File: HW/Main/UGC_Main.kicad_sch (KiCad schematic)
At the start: 147 parts, among them J1 Rumble, J1 USB4105-GF-A-060, J10 Conn_01x01_Pin, J11 Conn_01x01_Pin, J12 Conn_01x01_Pin, J2 LT, J3 RT, J5 Conn_01x01_Pin, J6 Conn_01x01_Pin, J7 Conn_01x01_Pin, J7 Conn_01x05_Pin, J8 Conn_01x01_Pin, J9 Conn_01x01_Pin, J9 Conn_01x05_Pin, Q1 MMBT3904, Q2 MMBT3904, Q3 BSS138DW, Q4 BSS138DW, Q5 Q_NMOS_GSD, Q6 Q_PMOS_GDS, Q7 Q_NMOS_GSD, SW1 SW_Push, SW10 SW_Push, SW11 SW_Push, SW12 SW_Push, SW13 SW_Push, SW14 TS09-63-25-R-260-SMT, SW2 SW_Push, SW3 SW_Push, SW4 SW_Push, SW5 SW_Push, SW6 GL18_SW, SW7 SW_Push, SW8 SW_Push, SW9 TS09-63-25-R-260-SMT, T1 36-8730, T2 36-8730, T3 36-8730, T4 36-8730, U1 ESP32-PICO-MINI-02, U10 ST_LSM6, U11 BQ25180, U12 CH340K, U13 PI3USB4000A, U14 GH39F (Hall SOT23), U15 GH39F (Hall SOT23), U16 GH39F (Hall SOT23), U17 GH39F (Hall SOT23), U2 GD25Q80EEIGR, U2 GH39F (Hall SOT23), U3 GH39F (Hall SOT23), U4 GH39F (Hall SOT23), U5 GH39F (Hall SOT23), U6 MCP3002, U7 MCP3002, U8 RP2040, Y1 Crystal_GND3

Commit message: Checkpoint 2
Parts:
- removed C23, C24, C25, C26, C4: .047u, Capacitor_SMD:C_0603_1608Metric_Pad1.08x0.95mm_HandSolder, symbol Device:C
- removed J7: Conn_01x05_Pin, hhl:molex_5034800540, symbol Connector:Conn_01x05_Pin
- removed J9: Conn_01x05_Pin, Connector_PinHeader_2.00mm:PinHeader_1x05_P2.00mm_Vertical, symbol Connector:Conn_01x05_Pin
- removed L2, L4, L6, L8: SK6805-EC-15, hhl:SK6805-EC-15, symbol progcc_v3:SK6805-EC-15
- removed R3, R39: 1k, Resistor_SMD:R_0201_0603Metric, symbol Device:R
- removed T1: 36-8730, hhl:KS_8730, symbol Connector:TestPoint
- removed T2, T3, T4: 36-8730, progcc_v3:KS_8730, symbol Connector:TestPoint
- removed TP1, TP2, TP3: TestPoint, TestPoint:TestPoint_Pad_D1.5mm, symbol Connector:TestPoint
- removed U14, U15, U16, U17, U4, U5: GH39F (Hall SOT23), progcc_v3:GH39F, symbol progcc_v3:GH39F (Hall SOT23)
- added C1: 47uF 6.3v, Capacitor_Tantalum_SMD:CP_EIA-3216-18_Kemet-A, symbol Device:C_Polarized
- added C2: 2.2uF, Capacitor_SMD:C_0603_1608Metric, symbol Device:C
- added D10, D9: CUS08F30, Diode_SMD:D_SOD-323_HandSoldering, symbol progcc_v3:CUS08F30
- added F1: Fuse, Fuse:Fuse_1206_3216Metric_Pad1.42x1.75mm_HandSolder, symbol Device:Fuse
- added J13: 503480-0640, hhl:5034800640, symbol hhl:503480-0640
- added J4: Conn_01x06_Pin, Connector_PinHeader_2.00mm:PinHeader_1x06_P2.00mm_Vertical, symbol Connector:Conn_01x06_Pin
- added R14: 10k, Resistor_SMD:R_0201_0603Metric, symbol Device:R_Small
- added TP5: TestPoint, TestPoint:TestPoint_Pad_D1.5mm, symbol Connector:TestPoint
- added U3: XC6222, hhl:SOT-89-5, symbol hhl:XC6222B331PR-G
- added U5: ST_LSM6, hhl:LGA14, symbol progcc_v3:ST_LSM6
- C3: value .047u -> 2.2uF; footprint Capacitor_SMD:C_0603_1608Metric_Pad1.08x0.95mm_HandSolder -> Capacitor_SMD:C_0603_1608Metric; LCSC C15849 -> (none)
- R36, R37, R38, R4: value 1k -> 75k; footprint Resistor_SMD:R_0201_0603Metric -> Resistor_SMD:R_0603_1608Metric
- U2, U3: footprint progcc_v3:GH39F -> hhl:GH39F
- renumbered L3 to L2, L5 to L3, L7 to L4
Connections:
- net LS_BUTTON is gone; now on net Pulldown_D: SW6.S1 (1), SW6.S2 (2)
- net SR_Pull is gone; now on net DD_Pull: D4.6 (K)
- net UART0_TX is gone; now on net VBUS_SYS: JP1.2 (B)
- net VBUS_PRE is gone; now on net +5V_PRE: D1.2 (A)
- net +3V3: now also R36.2, R38.2, RV1.1 (GND), RV2.1 (GND), C1.1, C2.1, D10.2 (A), D9.1 (K), J13.6, J4.6 (Pin_6), TP5.1, U3.5 (Vout), U5.5 (VDDIO), U5.8 (VDD)
- net +5V: now also C16.1, D1.1 (K), JP1.1 (A), U11.A2 (IN); no longer J1.A4_B9 (VBUS), J1.B4_A9 (VBUS)
- net A_Pull: now also D1.6 (K), SW1.2; no longer D3.4 (K)
- net BAT_LVL: now also U8.40 (GPIO28_ADC2); no longer JP1.1 (A), U8.38 (GPIO26_ADC0)
- net BTN_PWR: now also U8.7 (GPIO5); no longer U8.16 (GPIO13)
- net B_Pull: now also D2.5 (K), SW2.2; no longer D5.6 (K)
- net D+: now also J7.1 (Pin_1)
- net D-: now also J9.1 (Pin_1)
- net DD_Pull: now also SW11.2; no longer D3.5 (K)
- net DL_Pull: now also D2.4 (K), SW12.2; no longer D5.5 (K)
- net DR_Pull: now also D5.5 (K), SW13.2; no longer D4.4 (K)
- net DU_Pull: now also D1.5 (K), SW10.2; no longer D2.6 (K)
- net ESP_EN: now also U8.38 (GPIO26_ADC0); no longer U8.18 (GPIO15)
- net GND: now also J5.1 (Pin_1), R37.1, R4.1, RV1.3 (V+), RV2.3 (V+), SW9.2, C1.2, C2.2, J13.1, J13.MP1, J13.MP2, J4.1 (Pin_1), U3.2 (GND), U5.2 (SDx), U5.3 (SCx), U5.6 (GNDIO), U5.7 (GND)
- net I2C_SCL: now also U8.35 (GPIO23); no longer U8.3 (GPIO1)
- net I2C_SDA: now also U8.34 (GPIO22); no longer U8.2 (GPIO0)
- net IMU0_CS: now also U8.2 (GPIO0); no longer U8.28 (GPIO17)
- net IMU1_CS: now also U8.4 (GPIO2), U5.12 (CS); no longer U8.32 (GPIO21)
- net LADC_CS: now also U8.3 (GPIO1); no longer U8.27 (GPIO16)
- net LX: no longer R36.2
- net LY: no longer R37.2
- net L_Pull: now also D1.4 (K), SW7.2; no longer D5.4 (K)
- net N_CLOCK: now also J6.1 (Pin_1)
- net N_CLOCK_3.3: now also U8.31 (GPIO20); no longer U8.5 (GPIO3)
- net N_DATA: now also J8.1 (Pin_1)
- net N_DATA_3.3: now also U8.30 (GPIO19); no longer U8.4 (GPIO2)
- net N_LATCH: now also J10.1 (Pin_1)
- net N_LATCH_3.3: now also U8.29 (GPIO18); no longer U8.6 (GPIO4)
- net Plus_Pull: now also D3.5 (K), SW5.2; no longer D1.5 (K)
- net RADC_CS: now also U8.12 (GPIO9); no longer U8.34 (GPIO22)
- net RGB_OUT: now also U8.32 (GPIO21); no longer U8.35 (GPIO23)
- net RUMBLE: now also U8.5 (GPIO3); no longer U8.36 (GPIO24)
- net RUMBLE-: now also J1.2 (Pin_2)
- net RX: now also J13.5, J4.5 (Pin_5); no longer C3.2, R38.2
- net RY: now also J13.4, J4.4 (Pin_4); no longer R4.2
- net R_BRAKE: now also U8.6 (GPIO4); no longer U8.37 (GPIO25)
- net R_Pull: now also D4.5 (K), SW8.2; no longer D3.6 (K)
- net SHARED_PU: now also D10.1 (K)
- net SL_Pull: now also D2.6 (K), SW6.S3 (3), SW6.S4 (4); no longer D2.4 (K)
- net SPI_CK: now also U8.8 (GPIO6), U5.13 (SCL); no longer U8.29 (GPIO18)
- net SPI_RX: now also U8.11 (GPIO8), U5.1 (SDO); no longer U8.31 (GPIO20)
- net SPI_TX: now also U8.9 (GPIO7), U5.14 (SDA); no longer U8.30 (GPIO19)
- net Scan_A: now also D1.1 (A), D1.2 (A), D1.3 (A), D2.1 (A), U8.16 (GPIO13); no longer U8.15 (GPIO12)
- net Scan_B: now also D2.2 (A), D2.3 (A), D3.1 (A), D3.2 (A), U8.15 (GPIO12); no longer U8.12 (GPIO9)
- net Scan_C: now also D3.3 (A), D4.1 (A), D4.2 (A), D4.3 (A), U8.14 (GPIO11); no longer U8.8 (GPIO6)
- net Scan_D: now also D5.1 (A), D5.2 (A), D5.3 (A), U8.13 (GPIO10); no longer U8.11 (GPIO8)
- net USB_EN: now also U8.36 (GPIO24); no longer U8.41 (GPIO29_ADC3)
- net USB_SEL: now also U8.37 (GPIO25); no longer U8.17 (GPIO14)
- net VBUS_SYS: now also C3.2, J1.1 (Pin_1), R14.2, U3.4 (Vin)
- net X_Pull: now also D3.4 (K), SW3.2; no longer D1.6 (K)
- net Y_Pull: now also D5.6 (K), SW4.2; no longer D2.5 (K)
- net ZL_ANALOG: now also R36.1, R4.2, RV1.2 (Signal), U8.41 (GPIO29_ADC3); no longer U8.39 (GPIO27_ADC1)
- net ZL_Pull: now also D3.6 (K), J2.1 (Pin_1); no longer D1.4 (K)
- net ZR_ANALOG: now also R37.2, R38.1, RV2.2 (Signal), U8.39 (GPIO27_ADC1); no longer U8.40 (GPIO28_ADC2)
- net ZR_Pull: now also D5.4 (K), J3.1 (Pin_1); no longer D4.5 (K)
- net Pulldown_C: now reaches J3.2 (Pin_2)
- net Pulldown_C: now also J2.2 (Pin_2), SW7.1, SW8.1, U8.27 (GPIO16)
- net Pulldown_A: now reaches SW1.1
- net Pulldown_A: now also SW2.1, SW3.1, SW4.1, U8.17 (GPIO14)
- net Pulldown_B: now reaches SW12.1
- net Pulldown_B: now also SW10.1, SW11.1, SW13.1, U8.18 (GPIO15)
- net +3V3_PRE: now reaches J12.1 (Pin_1)
- net +3V3_PRE: now also F1.2
- net +5V_PRE: now reaches J11.1 (Pin_1)
- net +5V_PRE: now also J1.A4_B9 (VBUS), J1.B4_A9 (VBUS)
- net Pulldown_D: now reaches SW5.1
- net Pulldown_D: now also U8.28 (GPIO17), J13.3, J4.3 (Pin_3)
- removed net Push_A: D1.1 (A), D1.2 (A), D1.3 (A), D2.1 (A), U8.7 (GPIO5)
- removed net Push_B: D2.2 (A), D2.3 (A), D3.1 (A), D3.2 (A), U8.9 (GPIO7)
- removed net Push_C: D3.3 (A), D4.1 (A), D4.2 (A), D4.3 (A), U8.13 (GPIO10)
- removed net Push_D: D5.1 (A), D5.2 (A), D5.3 (A), U8.14 (GPIO11)
- new net: R14.1, U3.1 (CE)
- new net: D9.2 (A), F1.1
- new net RS_B_IN: D4.4 (K), J13.2, J4.2 (Pin_2)
- no-connect marks 4 -> 8
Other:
- note added: "IMU 1"
- note added: "Input Matrix: One of the pulldowns is pulled to ground or set LOW. The others are set HIGH. When a button is pressed, the corresponding SCAN pin is pulled low, allowing for an indication of which button has been pressed according to which pulldown pin is active."
- note added: "LS"
- note added: "Power Bus"
- note removed: "Rumble Connection"
- moved on the sheet: C1, C10, C2, D1A, D1B, D1C, D2A, D2B, D2C, D3A, D3B, D3C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

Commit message: Updates
- Stick PCB
- USB C pcb
- trigger PCB
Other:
- moved on the sheet: C12, C13, U10, U5

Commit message: Production files
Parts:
- J1, J2, J3, SW1, SW10, SW11, SW12, SW13, SW2, SW3, SW4, SW5: now not fitted; now left out of the parts list
- J10, J11, J12, J5, J6, J7, J8, J9: MPN (none) -> YZ72015053P-01
- J13: MPN (none) -> 503480-0640; Manufacturer_Part_Number 503480-0640 -> (none)
- SW7, SW8: MPN (none) -> TC-00100V H5.0 100gf
- U1: MPN (none) -> ESP32-PICO-MINI-02
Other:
- note added: "Analog Triggers"
- note added: "Internal USB"
- moved on the sheet: B1, C1, C12, C13, C14, C15, C16, C17, C18, C2, C20, C21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

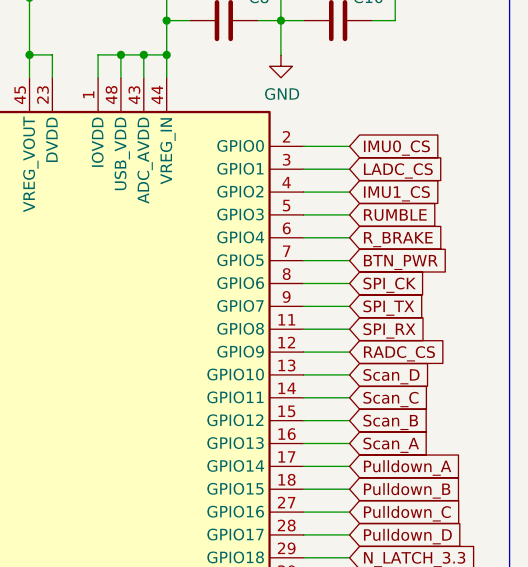
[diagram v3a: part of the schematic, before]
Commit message: Update
- Add initial firmware
- Fix PCB trace for SPI RX pin
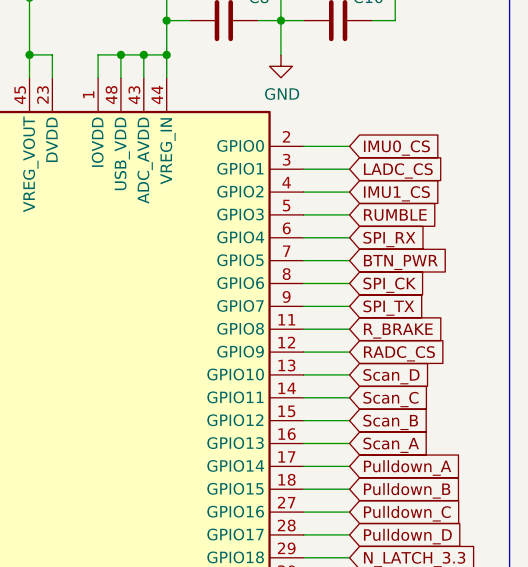
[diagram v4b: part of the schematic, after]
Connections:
- net R_BRAKE: now also U8.11 (GPIO8); no longer U8.6 (GPIO4)
- net SPI_RX: now also U8.6 (GPIO4); no longer U8.11 (GPIO8)
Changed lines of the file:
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@@
-    )
-  )
-  (global_label "SPI_RX" (shape input) (at 388.62 179.07 0) (fields_autoplaced)
-    (effects (font (size 1.27 1.27)) (justify left))
-    (property "Intersheetrefs" "${INTERSHEET_REFS}" (at 397.403 179.07 0)
-      (effects (font (size 1.27 1.27)) (justify left) hide)
     )
   )
@@
     )
   )
-  (global_label "R_BRAKE" (shape input) (at 388.62 168.91 0) (fields_autoplaced)
-    (effects (font (size 1.27 1.27)) (justify left))
-    (property "Intersheetrefs" "${INTERSHEET_REFS}" (at 399.2294 168.9894 0)
-      (effects (font (size 1.27 1.27)) (justify left) hide)
-    )
-  )
   (global_label "+3V3_PRE" (shape input) (at 114.3 207.01 0) (fields_autoplaced)
     (effects (font (size 1.27 1.27)) (justify left))
@@
     )
   )
+  (global_label "SPI_RX" (shape input) (at 388.62 168.91 0) (fields_autoplaced)
+    (effects (font (size 1.27 1.27)) (justify left))
+    (property "Intersheetrefs" "${INTERSHEET_REFS}" (at 397.403 168.91 0)
+      (effects (font (size 1.27 1.27)) (justify left) hide)
+    )
+  )
   (global_label "RUMBLE-" (shape input) (at 273.05 173.99 0) (fields_autoplaced)
     (effects (font (size 1.27 1.27)) (justify left))
@@
       (effects (font (size 1.27 1.27)) (justify left) hide)
     )
+  )
+  (global_label "R_BRAKE" (shape input) (at 388.62 179.07 0) (fields_autoplaced)
+    (effects (font (size 1.27 1.27)) (justify left))
+    (property "Intersheetrefs" "${INTERSHEET_REFS}" (at 399.2294 179.1494 0)
+      (effects (font (size 1.27 1.27)) (justify left) hide)
+    )

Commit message: Power update
- Update regulator
- Add relevant components
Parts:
- removed D10: CUS08F30, Diode_SMD:D_SOD-323_HandSoldering, symbol progcc_v3:CUS08F30
- removed R14: 10k, Resistor_SMD:R_0201_0603Metric, symbol Device:R_Small
- removed U3: XC6222, hhl:SOT-89-5, symbol hhl:XC6222B331PR-G
- added L5: 1.3A 2.2uH ±20% 80mΩ, Inductor_SMD:L_1008_2520Metric, symbol Device:L
- added U4: TPS630001RCR, hhl:VREG_V62_16624-01YE, symbol hhl:TPS63000DRCR
- B1: symbol hhl:Conn_01x02_Male -> Connector:Conn_01x02_Pin
- C2, C3: value 2.2uF -> 10uF; footprint Capacitor_SMD:C_0603_1608Metric -> Capacitor_SMD:C_0805_2012Metric
- J13: Manufacturer_Part_Number (none) -> 503480-0640
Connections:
- net +3V3: now also C3.1, U4.1 (VOUT), U4.10 (FB); no longer C1.1, C2.1, D9.1 (K)
- net GND: now also C2.1, C3.2, U4.11 (EP), U4.11_1 (EP), U4.11_2 (EP), U4.11_3 (EP), U4.11_4 (EP), U4.11_5 (EP), U4.11_6 (EP), U4.11_7 (EP), U4.11_8 (EP), U4.3 (PGND), U4.9 (GND); no longer C2.2, C3.1
- net VBUS_SYS: now also C2.2, D9.1 (K), U4.5 (VIN), U4.6 (EN), U4.7 (PS/SYNC), U4.8 (VINA); no longer C3.2
- net at D9.2 (A), F1.1: now also C1.1
- net +5V renamed VBUS
- new net: L5.1, U4.4 (L1)
- new net: L5.2, U4.2 (L2)
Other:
- moved on the sheet: C1, C2, J10, J11, J12, J5, J6, J7, J8, J9, R1, R2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

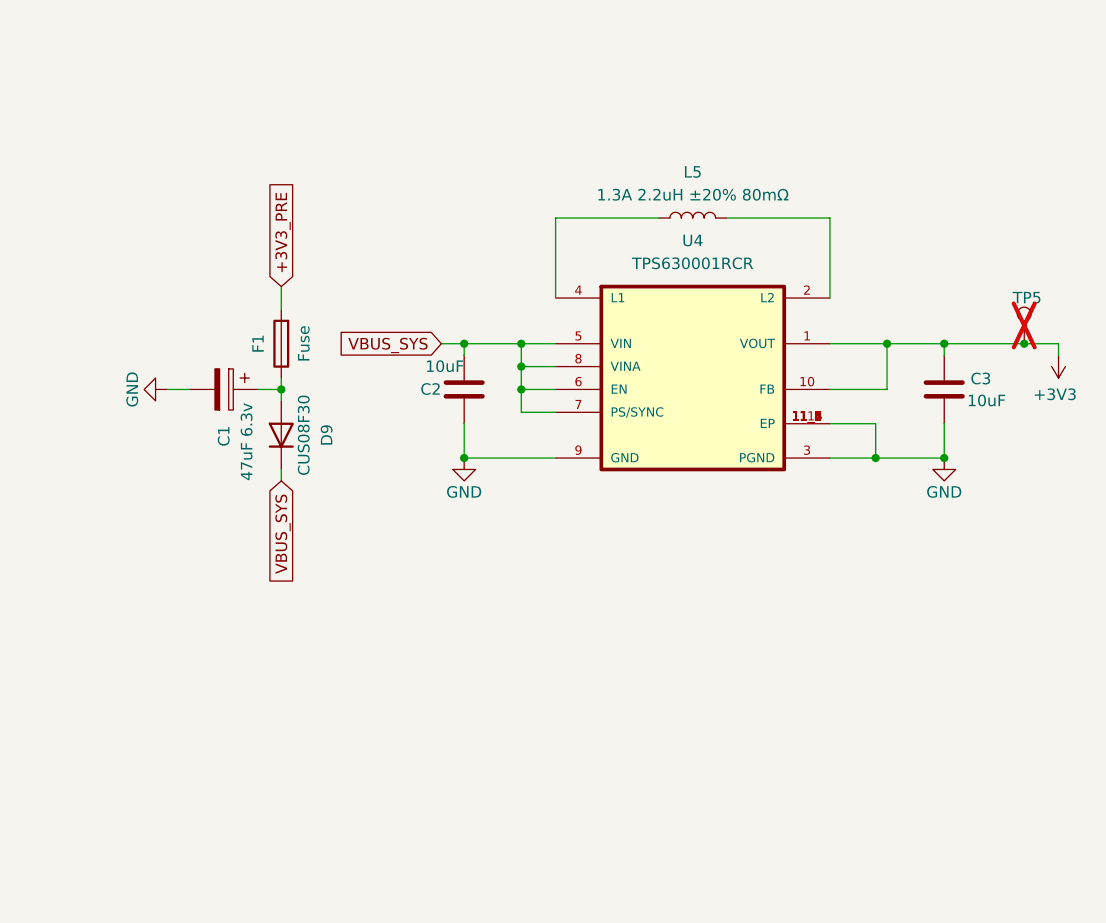
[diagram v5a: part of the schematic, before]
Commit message: Update
- Remove 3d files
- Update power regulator and schematic
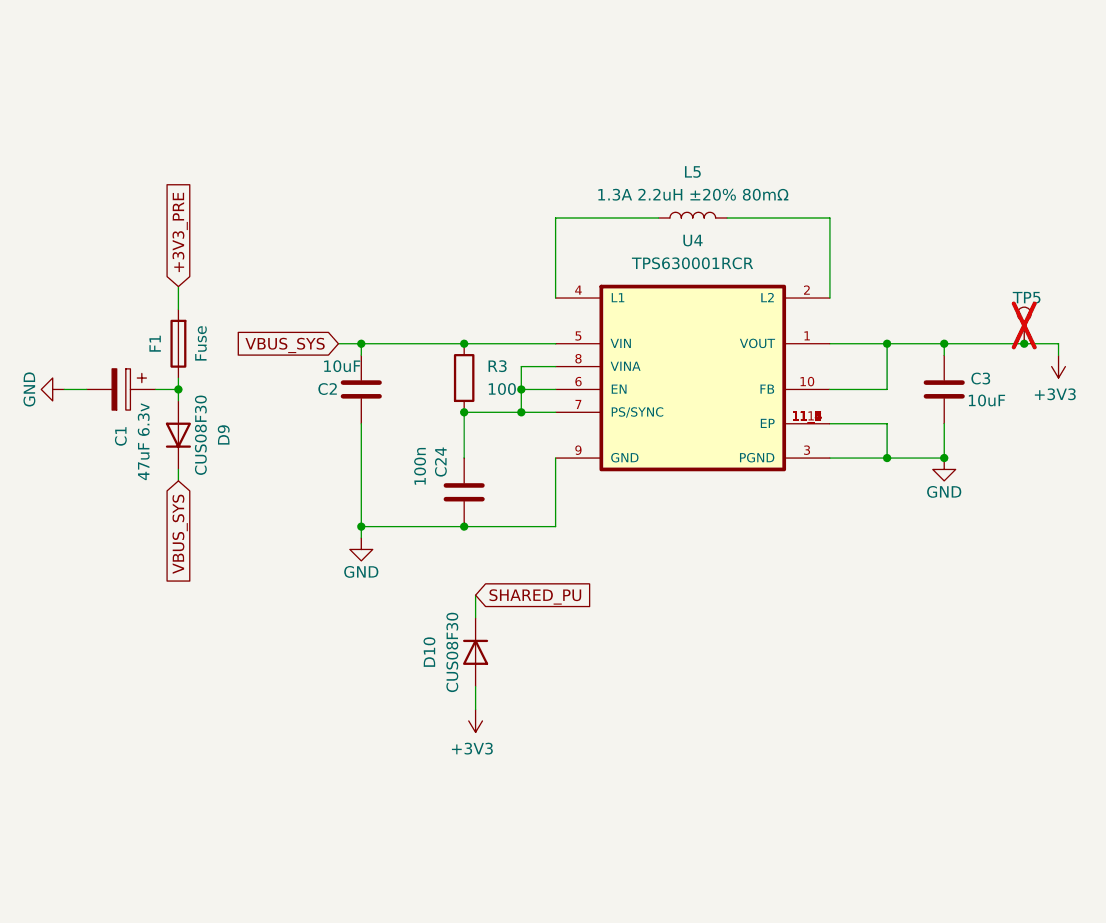
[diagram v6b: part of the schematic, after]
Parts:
- added C24: 100n, Capacitor_SMD:C_0201_0603Metric, symbol Device:C
- added D10: CUS08F30, Diode_SMD:D_SOD-323_HandSoldering, symbol progcc_v3:CUS08F30
- added R3: 100, Resistor_SMD:R_0201_0603Metric, symbol Device:R
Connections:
- net +3V3: now also D10.2 (A)
- net GND: now also C24.1
- net SHARED_PU: now also D10.1 (K)
- net VBUS_SYS: now also R3.1; no longer U4.6 (EN), U4.7 (PS/SYNC), U4.8 (VINA)
- new net: C24.2, R3.2, U4.6 (EN), U4.7 (PS/SYNC), U4.8 (VINA)
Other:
- moved on the sheet: C1, C2, D9, F1

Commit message: Unify USB C connector
Unified USB-C Connection
Reliability issues present with type C pogo pin board
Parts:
- removed J1: USB4105-GF-A-060, hhl:GCT_USB4105-GF-A-060, symbol hhl:USB4105-GF-A-060
- removed J10, J11, J12, J5, J6, J7, J8, J9: Conn_01x01_Pin, hhl:YZ72015053P-01, symbol Connector:Conn_01x01_Pin
- removed R5, R6: 5.1k, Resistor_SMD:R_0201_0603Metric, symbol Device:R_Small
- added J5: UJ31-CH-G1-SMT-TR, hhl:CUI_UJ31-CH-G1-SMT-TR, symbol hhl:UJ31-CH-G1-SMT-TR
- added R21, R22: 5.1kohm, Resistor_SMD:R_0603_1608Metric, symbol Device:R
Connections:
- net +3V3_PRE: now also J5.A2 (SSTXP1), J5.B2 (SSTXP2)
- net +5V_PRE: now also J5.A4 (VBUS), J5.A9 (VBUS), J5.B4 (VBUS), J5.B9 (VBUS)
- net D+: now also J5.A6 (DP1), J5.B6 (DP2)
- net D-: now also J5.A7 (DN1), J5.B7 (DN2)
- net GND: now also J5.A1 (GND), J5.A12 (GND), J5.B1 (GND), J5.B12 (GND), J5.SH1 (SHIELD), J5.SH2 (SHIELD), J5.SH3 (SHIELD), J5.SH4 (SHIELD), J5.SH5 (SHIELD), J5.SH6 (SHIELD), R21.1, R22.1
- net N_CLOCK: now also J5.A3 (SSTXN1), J5.B3 (SSTXN2)
- net N_DATA: now also J5.A11 (SSRXP2), J5.B11 (SSRXP1)
- net N_LATCH: now also J5.A10 (SSRXN2), J5.B10 (SSRXN1)
- new net CC1: J5.A5 (CC1), R21.2
- new net CC2: J5.B5 (CC2), R22.2
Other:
- note removed: "Internal USB"
- note removed: "USB POGO"

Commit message: PCB Update
- Add RESET switch
- Add ESP bootloader switch
- Adjust screw holes for trigger bracket mount
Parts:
- added SW1 (x2): 1TS026A-1000-0550, hhl:1TS026A-1000-0550, symbol hhl:1TS026A-1000-0550
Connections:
- net ESP_IO0: now also SW1.3, SW1.4
- net GND: now also SW1.1, SW1.1, SW1.2, SW1.2
- net USB_BOOT: now also SW1.3, SW1.4; no longer SW14.2
- net RUN renamed RP_RUN
- net RP_RUN: now also SW14.2
